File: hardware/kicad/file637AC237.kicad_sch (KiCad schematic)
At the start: 45 parts, among them J1 Data, J2 Power, J3 Input, Q1 VN10N, Q2 2SK2394, Q3 2SK2394, T1 Input, U1 AP1117-50, U2 Si5351Module, U3 FST3253

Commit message: Firmware: encoder ISR queue, S-meter calibration, UI polish, SI5351 fixes
Firmware changes:
- RotaryInput: rewrite to interrupt-driven ISR queue (RP2040 GPIO callback,
  64-event ring buffer). Eliminates ~2-3 step/sec polling limit.
- SI5351Control: add liveRetune param to setQuadrature90(). Live-retune path
  skips PLL reset and output disable/enable to eliminate audio transients.
  Both CLK0/CLK1 forced to PLLA for phase coherence. Phase registers zeroed
  in all low-band paths.
- BoardControl: S-meter ADC inversion (higher V = weaker signal), configurable
  zero-raw floor, gain permille, and optional sqrt log companding.
- main.cpp: analogReadResolution(12) for 12-bit ADC. S_METER_ZERO_RAW=372
  (~3V floor), GAIN=1220, LOG=true. Tune coalescing via flushPendingTuneDelta.
  40ms display refresh throttle. S-meter suppressed during tuning (120ms).
  LED steady on (no heartbeat). SI5351 correction -4610000 PPB.
- DisplayUI: step indicator label, flashTuneDirection (UP/DN), step digit
  flash with 500ms duration on encoder button press.
- upload_uf2.py: wait-for-mount loop + picotool fallback upload.

Hardware:
- KiCAD PCB and schematic updates (mixer sheet, audio sheet)
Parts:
- removed C2, C4: 1n, Capacitor_SMD:C_0805_2012Metric, symbol Device:C
- removed C3: 10u, Capacitor_SMD:CP_Elec_3x5.3, symbol QRPTransceiver-rescue:CP-Device
- removed C5, C7, C8, C9: 100n, Capacitor_SMD:C_0805_2012Metric, symbol Device:C
- removed L1: 100n, Inductor_SMD:L_0805_2012Metric, symbol Device:L
- removed L2: 1n, Inductor_SMD:L_0805_2012Metric, symbol Device:L
- removed L3: 500u, Inductor_SMD:L_0805_2012Metric, symbol Device:L
- removed Q1: VN10N, Package_TO_SOT_SMD:SOT-23, symbol Simulation_SPICE:NMOS
- removed Q2, Q3: 2SK2394, Package_TO_SOT_SMD:SC-59, symbol Simulation_SPICE:NJFET
- removed R1, R3: 47, Resistor_SMD:R_0805_2012Metric, symbol Device:R
- removed R10, R4, R5: 10K, Resistor_SMD:R_0805_2012Metric, symbol Device:R
- removed R2: 100, Resistor_SMD:R_0805_2012Metric, symbol Device:R
- removed R6, R7: 1K, Resistor_SMD:R_0805_2012Metric, symbol Device:R
- removed R8, R9: 1M, Resistor_SMD:R_0805_2012Metric, symbol Device:R
- added C110, C111: 100p, symbol Device:C
- added C112: 220p, Capacitor_SMD:C_0805_2012Metric, symbol Device:C
- added C113, C114, C115: 100n, symbol Device:C
- added C9: 10u, Capacitor_SMD:CP_Elec_3x5.3, symbol QRPTransceiver-rescue:CP-Device
- added L4: 100n, symbol Device:L
- added L5: 500u, symbol Device:L
- added Q10, Q9: J310, symbol Simulation_SPICE:NJFET
- added Q11: 2N3904, symbol Simulation_SPICE:NPN
- added R114: 100R, symbol Device:R
- added R115: 47R, symbol Device:R
- added R116, R118: 10K, symbol Device:R
- added R117: 1M, symbol Device:R
- added R119: 3.3K, symbol Device:R
- added R120, R121: 33K, symbol Device:R
- added R122: 2.2K, symbol Device:R
- D1: footprint Diode_SMD:D_1206_3216Metric -> Diode_SMD:D_1210_3225Metric_Pad1.42x2.65mm_HandSolder
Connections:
- net VREF is gone; now on net +5V: J2.4 (Pin_4)
- net +12V: now also C6.1
- net +5V: now also C10.1, J2.5 (Pin_5), C9.1; no longer C6.1, J2.6 (Pin_6)
- net CWMUTE: now also J1.3 (Pin_3); no longer J1.4 (Pin_4)
- net GND: now also C10.2, C110.2, C111.2, C113.1, C114.2, C9.2, R115.2, R116.1, R117.2, R119.2, R121.2, R122.2
- net SMETER: now also J1.4 (Pin_4); no longer J1.2 (Pin_2)
- net SSBMUTE: now also J1.2 (Pin_2); no longer J1.3 (Pin_3)
- net at D1.2 (A), J2.1 (Pin_1): now also J2.3 (Pin_3); no longer J2.2 (Pin_2)
- net at C1.2: now also C110.1, L4.1, R114.1
- net at C11.1, R11.1: now also L5.1, Q11.1 (C), R118.1, R120.1
- net at C12.1: now also Q11.3 (E), R122.1
- new net: C111.1, C112.1, L4.2, R114.2, R115.1
- new net: C114.1, Q10.1 (S), R119.1
- new net: C112.2, Q10.3 (G), R117.1
- new net: C113.2, Q9.3 (G), R116.2, R118.2
- new net: C115.2, Q11.2 (B), R120.2, R121.1
- new net: Q10.2 (D), Q9.1 (S)
- new net: C115.1, L5.2, Q9.2 (D)

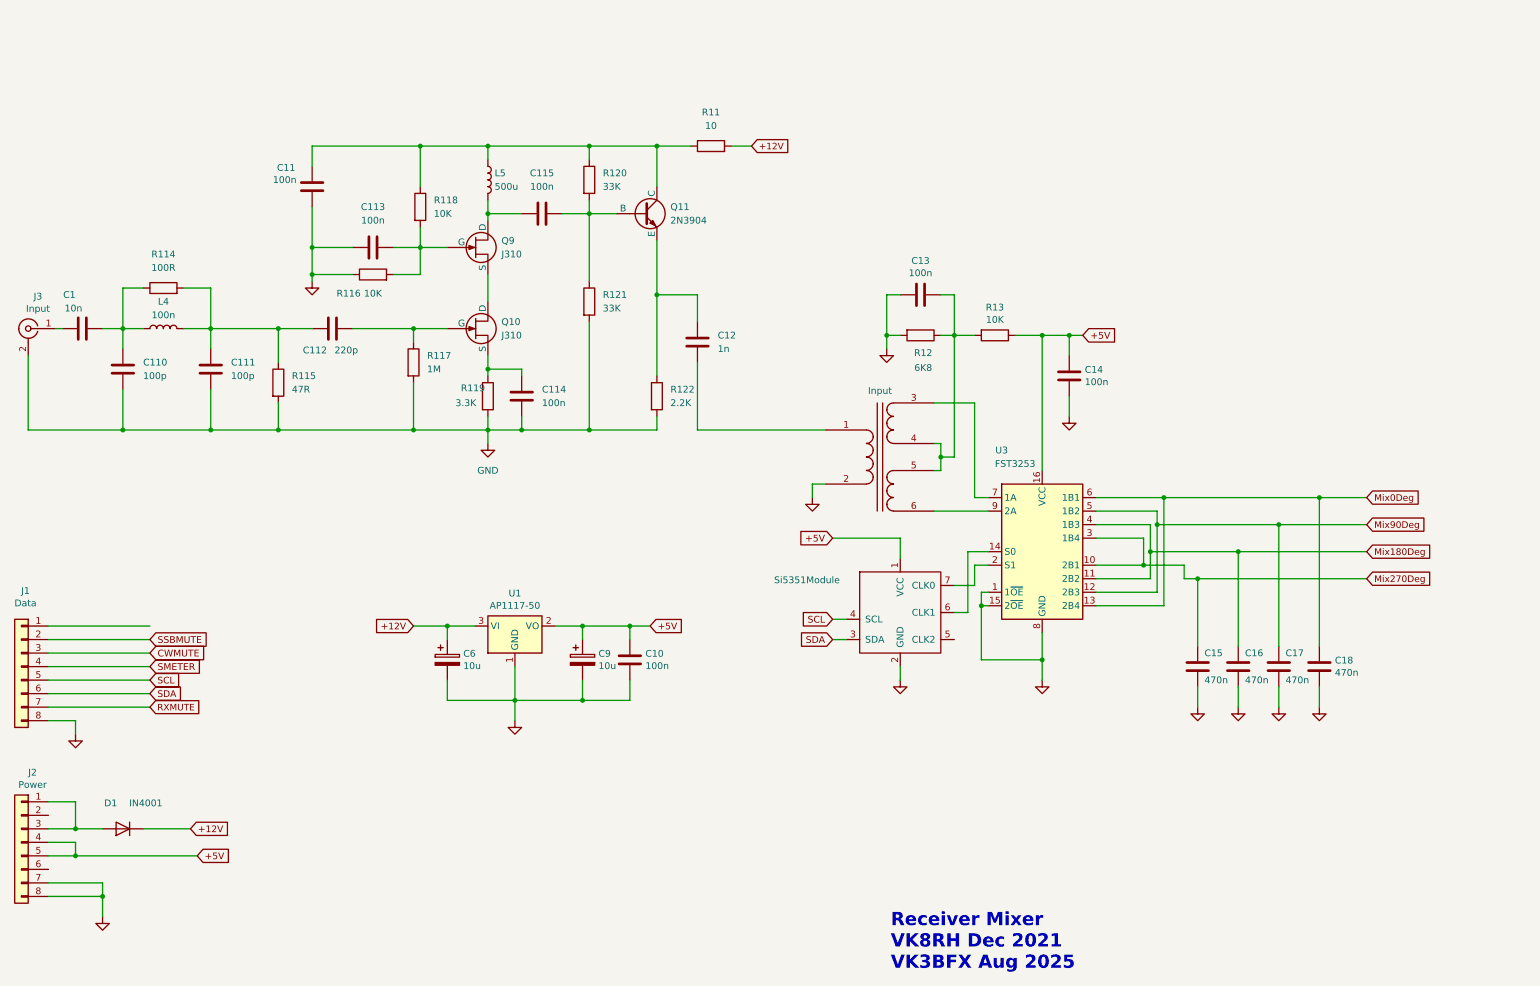
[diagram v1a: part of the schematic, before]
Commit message: Fixed quadrature generation PCB excirt circuit in draft
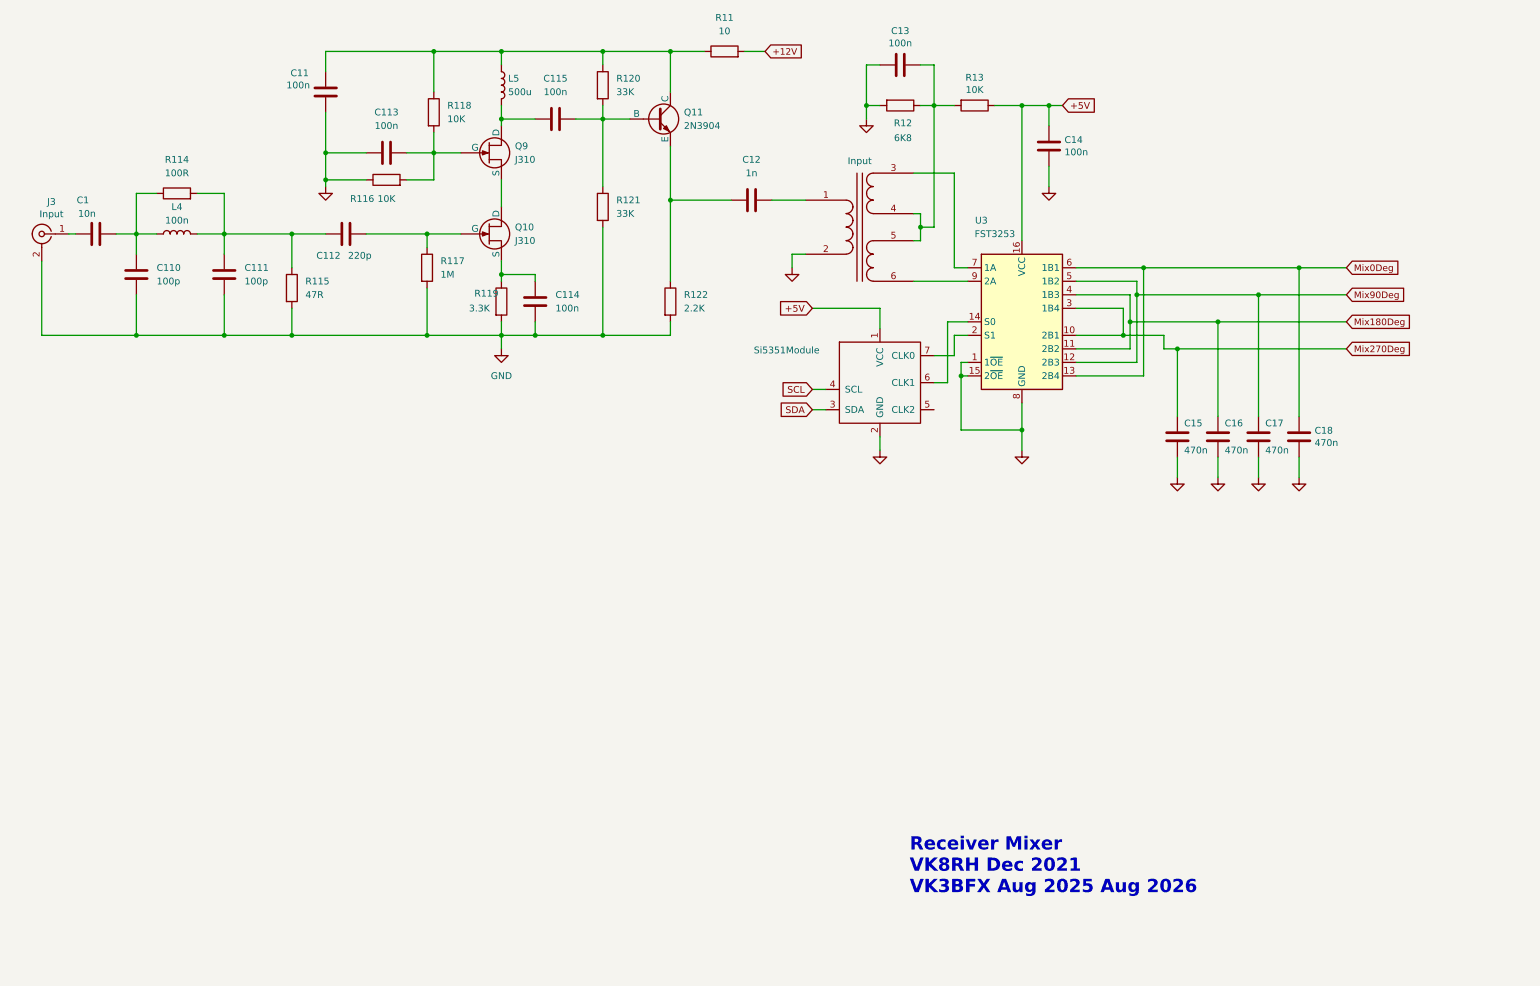
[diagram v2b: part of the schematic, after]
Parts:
- removed C10: 100n, Capacitor_SMD:C_0805_2012Metric, symbol Device:C
- removed C6, C9: 10u, Capacitor_SMD:CP_Elec_3x5.3, symbol QRPTransceiver-rescue:CP-Device
- removed D1: IN4001, Diode_SMD:D_1210_3225Metric_Pad1.42x2.65mm_HandSolder, symbol Device:D
- removed J1: Data, Connector_PinHeader_2.54mm:PinHeader_1x08_P2.54mm_Vertical, symbol Connector_Generic:Conn_01x08
- removed J2: Power, Connector_PinHeader_2.54mm:PinHeader_1x08_P2.54mm_Vertical, symbol Connector_Generic:Conn_01x08
- removed U1: AP1117-50, Package_TO_SOT_SMD:SOT-223-3_TabPin2, symbol Regulator_Linear:AP1117-50
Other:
- note added: "Receiver Mixer VK8RH Dec 2021 VK3BFX Aug 2025 Aug 2026"
- note removed: "Receiver Mixer VK8RH Dec 2021 VK3BFX Aug 2025"
- moved on the sheet: C1, C11, C110, C111, C112, C113, C114, C115, C12, C13, C14, C15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
